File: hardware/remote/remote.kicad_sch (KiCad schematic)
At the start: 25 parts

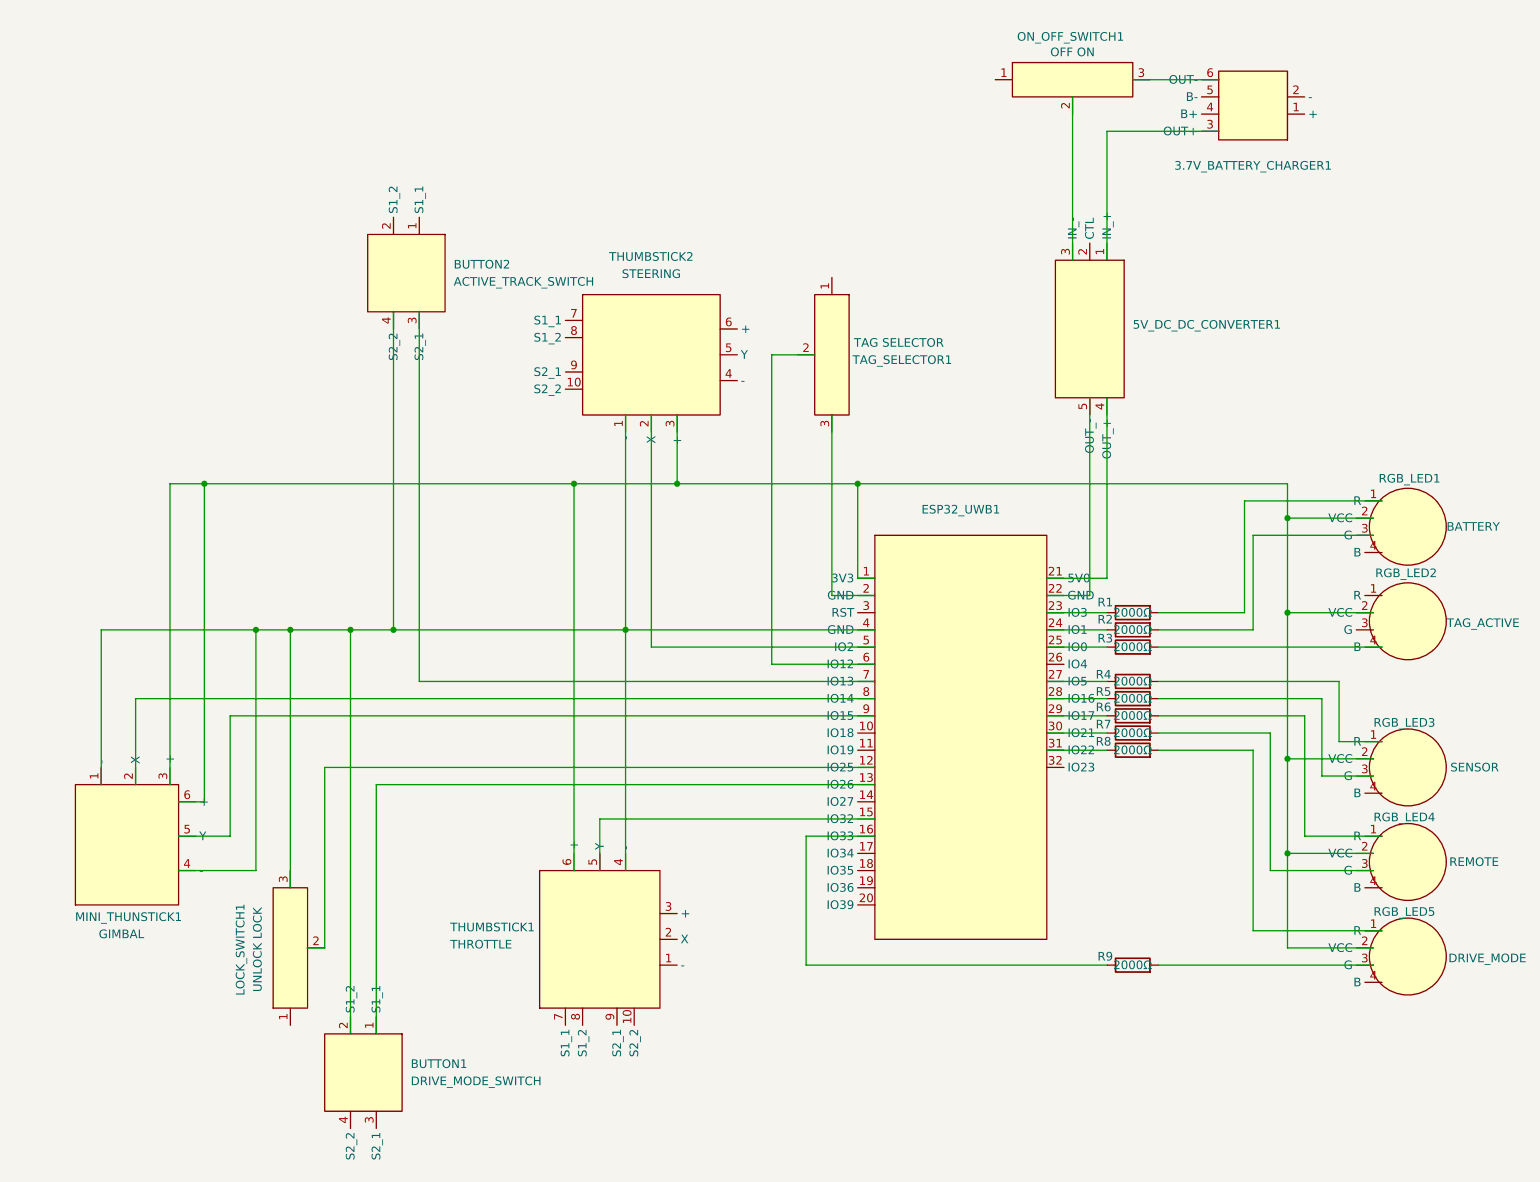
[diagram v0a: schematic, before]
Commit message: remote: Add battery status LED logic.
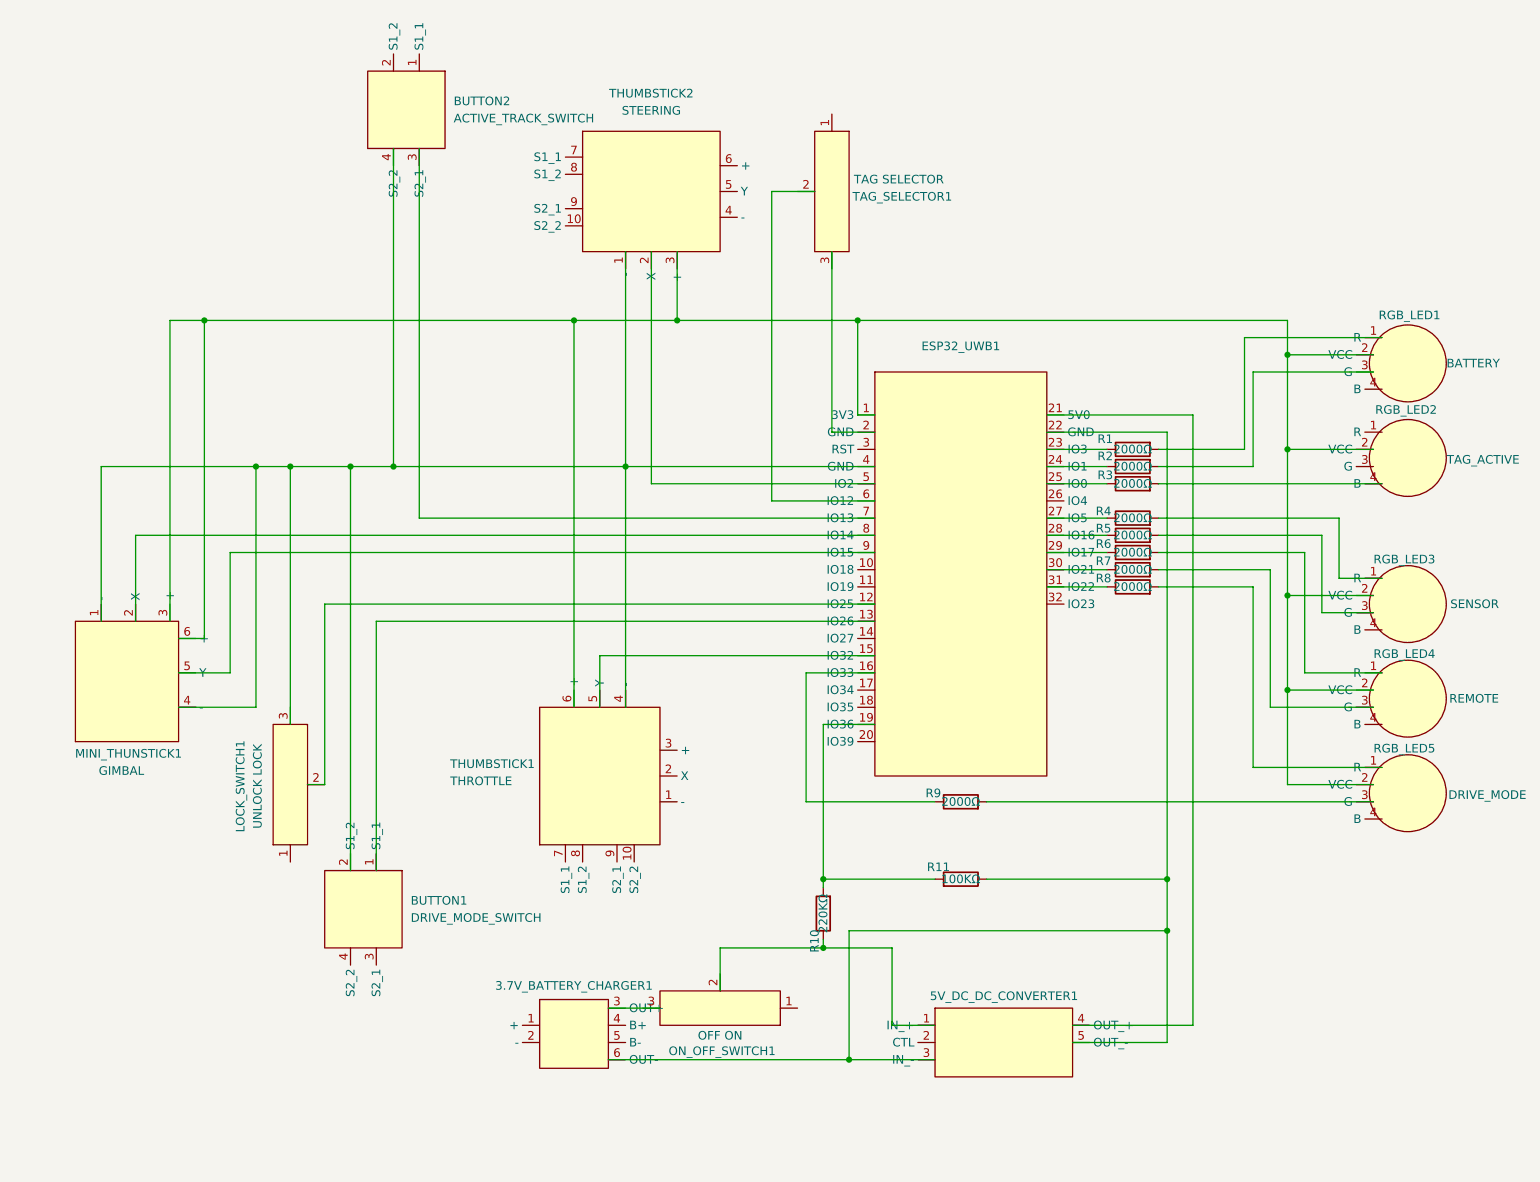
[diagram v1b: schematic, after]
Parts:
- added R10: 220KΩ, Autocam:Simple Resistor, symbol Autocam:Simple Resistor
- added R11: 100KΩ, Autocam:Simple Resistor, symbol Autocam:Simple Resistor
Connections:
- net at 3.7V_BATTERY_CHARGER1.3 (OUT+): now also ON_OFF_SWITCH1.3; no longer 5V_DC_DC_CONVERTER1.1 (IN_+)
- net at 3.7V_BATTERY_CHARGER1.6 (OUT-): now also 5V_DC_DC_CONVERTER1.3 (IN_-), 5V_DC_DC_CONVERTER1.5 (OUT_-), ESP32_UWB1.22 (GND), R11.1; no longer ON_OFF_SWITCH1.3
- net at ON_OFF_SWITCH1.2: now also 5V_DC_DC_CONVERTER1.1 (IN_+), R10.1; no longer 5V_DC_DC_CONVERTER1.3 (IN_-)
- net at ESP32_UWB1.19 (IO36): now also R10.2, R11.2
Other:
- moved on the sheet: 3.7V_BATTERY_CHARGER1, 5V_DC_DC_CONVERTER1, BUTTON1, BUTTON2, ESP32_UWB1, LOCK_SWITCH1, MINI_THUNSTICK1, ON_OFF_SWITCH1, R1, R2, R3, R4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

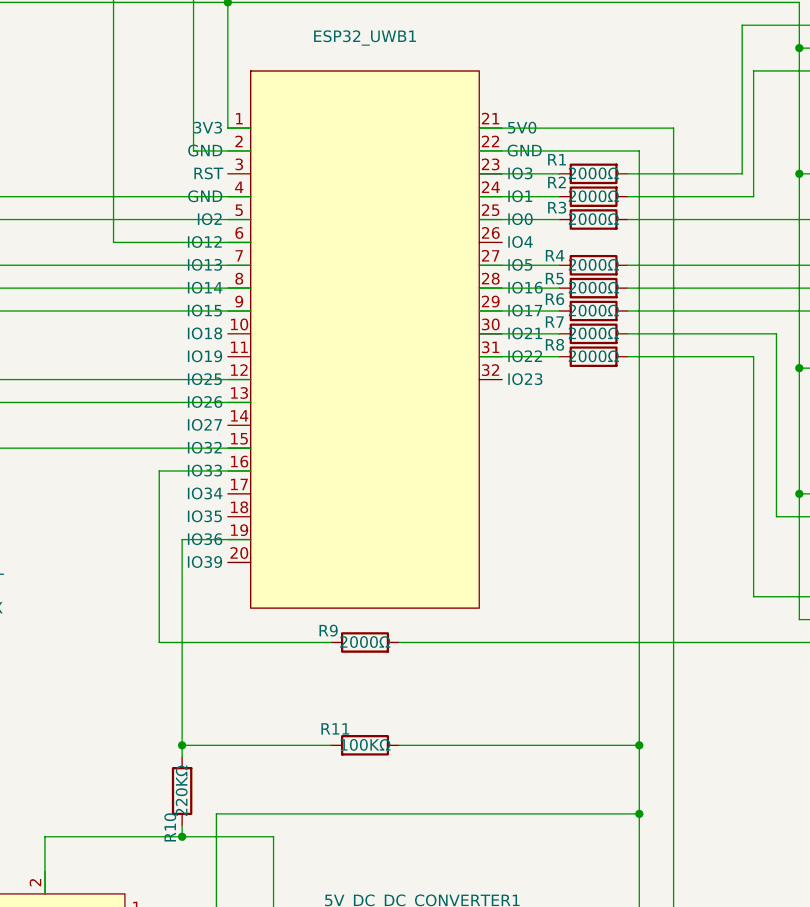
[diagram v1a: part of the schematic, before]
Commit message: hardware: Increase the LED resistor from 2000Ω to 10KΩ.
To reduce the power consumption.
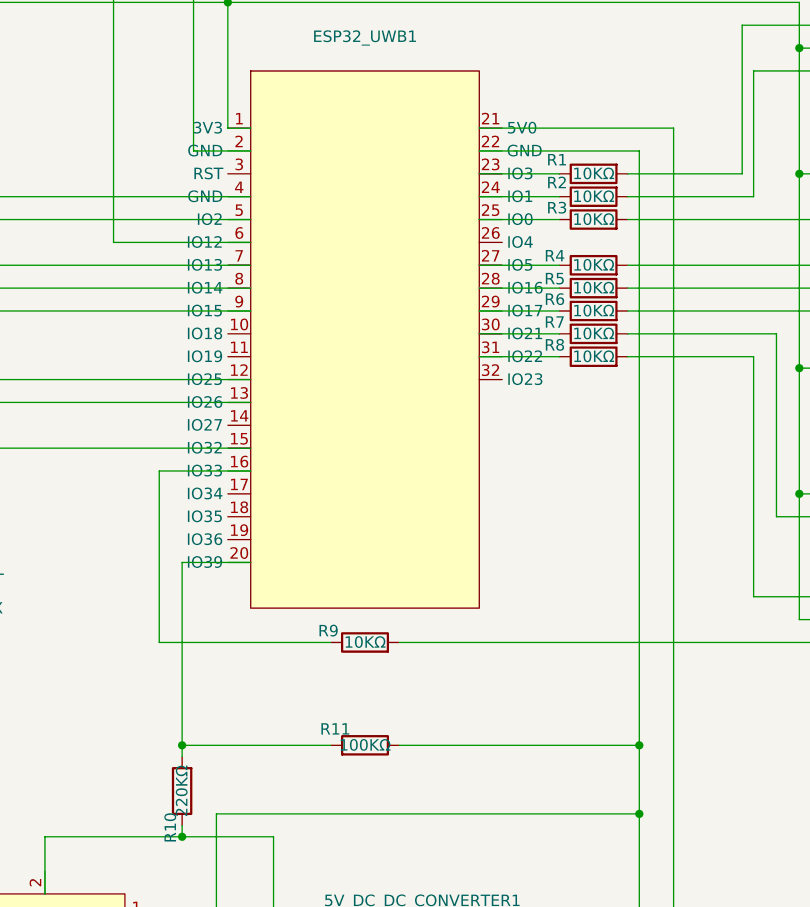
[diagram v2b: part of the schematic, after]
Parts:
- R1, R2, R3, R4, R5, R6, R7, R8, R9: value 2000Ω -> 10KΩ
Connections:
- net at R10.2, R11.2: now also ESP32_UWB1.20 (IO39); no longer ESP32_UWB1.19 (IO36)
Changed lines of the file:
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@@
+	(wire
+		(pts
+			(xy 134.62 120.65) (xy 134.62 140.97)
+		)
+		(stroke
+			(width 0)
+			(type default)
+		)
+	)
 	(wire
 		(pts
@@
 	(wire
 		(pts
-			(xy 134.62 118.11) (xy 134.62 140.97)
-		)
-		(stroke
-			(width 0)
-			(type default)
-		)
-	)
-	(wire
-		(pts
 			(xy 142.24 92.71) (xy 46.99 92.71)
 		)
@@
 	(wire
 		(pts
+			(xy 134.62 120.65) (xy 142.24 120.65)
+		)
+		(stroke
+			(width 0)
+			(type default)
+		)
+	)
+	(wire
+		(pts
 			(xy 132.08 129.54) (xy 132.08 110.49)
 		)
@@
 		(pts
 			(xy 217.17 124.46) (xy 198.12 124.46)
-		)
-		(stroke
-			(width 0)
-			(type default)
-		)
-	)
-	(wire
-		(pts
-			(xy 142.24 118.11) (xy 134.62 118.11)
 		)
 		(stroke
@@
 			)
 		)
-		(property "Value" "2000Ω"
+		(property "Value" "10KΩ"
 			(at 180.34 82.55 90)
 			(effects
@@
 			)
 		)
-		(property "Value" "2000Ω"
+		(property "Value" "10KΩ"
 			(at 180.34 80.01 90)
 			(effects
@@
 			)
 		)
-		(property "Value" "2000Ω"
+		(property "Value" "10KΩ"
 			(at 180.34 97.79 90)
 			(effects
@@
 			)
 		)
-		(property "Value" "2000Ω"
+		(property "Value" "10KΩ"
 			(at 154.94 129.54 90)
 			(effects
@@
 			)
 		)
-		(property "Value" "2000Ω"
+		(property "Value" "10KΩ"
 			(at 180.34 90.17 90)
 			(effects
@@
 			)
 		)
-		(property "Value" "2000Ω"
+		(property "Value" "10KΩ"
 			(at 180.34 87.63 90)
 			(effects
@@
 			)
 		)
-		(property "Value" "2000Ω"
+		(property "Value" "10KΩ"
 			(at 180.34 77.47 90)
 			(effects
@@
 			)
 		)
-		(property "Value" "2000Ω"
+		(property "Value" "10KΩ"
 			(at 180.34 95.25 90)
 			(effects
@@
 			)
 		)
-		(property "Value" "2000Ω"
+		(property "Value" "10KΩ"
 			(at 180.34 92.71 90)
 			(effects

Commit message: remote: Add UWB selector switch.
This switch will choose whether to use tag or the remote for the
distance measurement.

Also updated the PIN number and moved all non-uwb task to a separate
core.
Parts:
- RGB_LED2: value TAG_ACTIVE -> UWB_SELECTED
- UWB_SELECTOR1: renamed from TAG_SELECTOR1; value TAG SELECTOR -> UWB SELECTOR
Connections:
- net at BUTTON1.2 (S1_2), BUTTON2.4 (S2_2), ESP32_UWB1.4 (GND)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: now also LOCK_SWITCH1.2; no longer LOCK_SWITCH1.3
- net at BUTTON1.1 (S1_1): no longer ESP32_UWB1.13 (IO26)
- net at BUTTON1.3 (S2_1): now also ESP32_UWB1.18 (IO35)
- net at ESP32_UWB1.12 (IO25): no longer LOCK_SWITCH1.2
- net at ESP32_UWB1.15 (IO32): now also LOCK_SWITCH1.3; no longer THUMBSTICK1.5 (Y)
- net at ESP32_UWB1.19 (IO36): now also THUMBSTICK1.5 (Y)
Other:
- moved on the sheet: BUTTON1, LOCK_SWITCH1, MINI_THUNSTICK1, THUMBSTICK1
